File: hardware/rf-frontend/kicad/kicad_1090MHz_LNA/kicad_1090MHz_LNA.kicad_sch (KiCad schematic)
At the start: 11 parts, among them IC1 PGA-103_, X1 STA1090EC

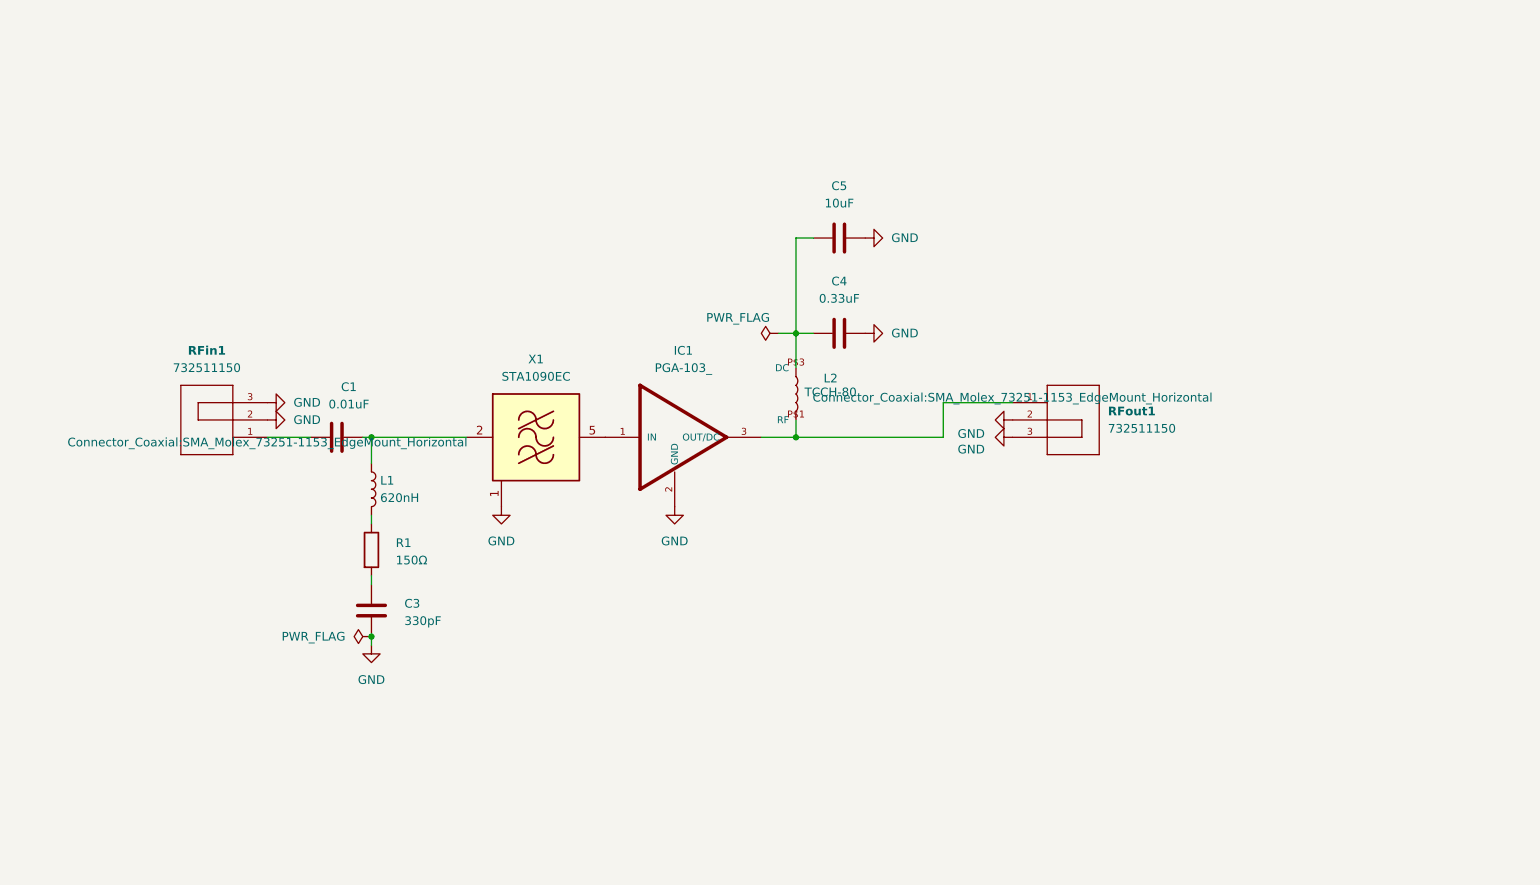
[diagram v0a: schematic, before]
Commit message: Update RF frontend KiCad: completed USB-C LNA board with routing, pours, via stitching, and Gerbers
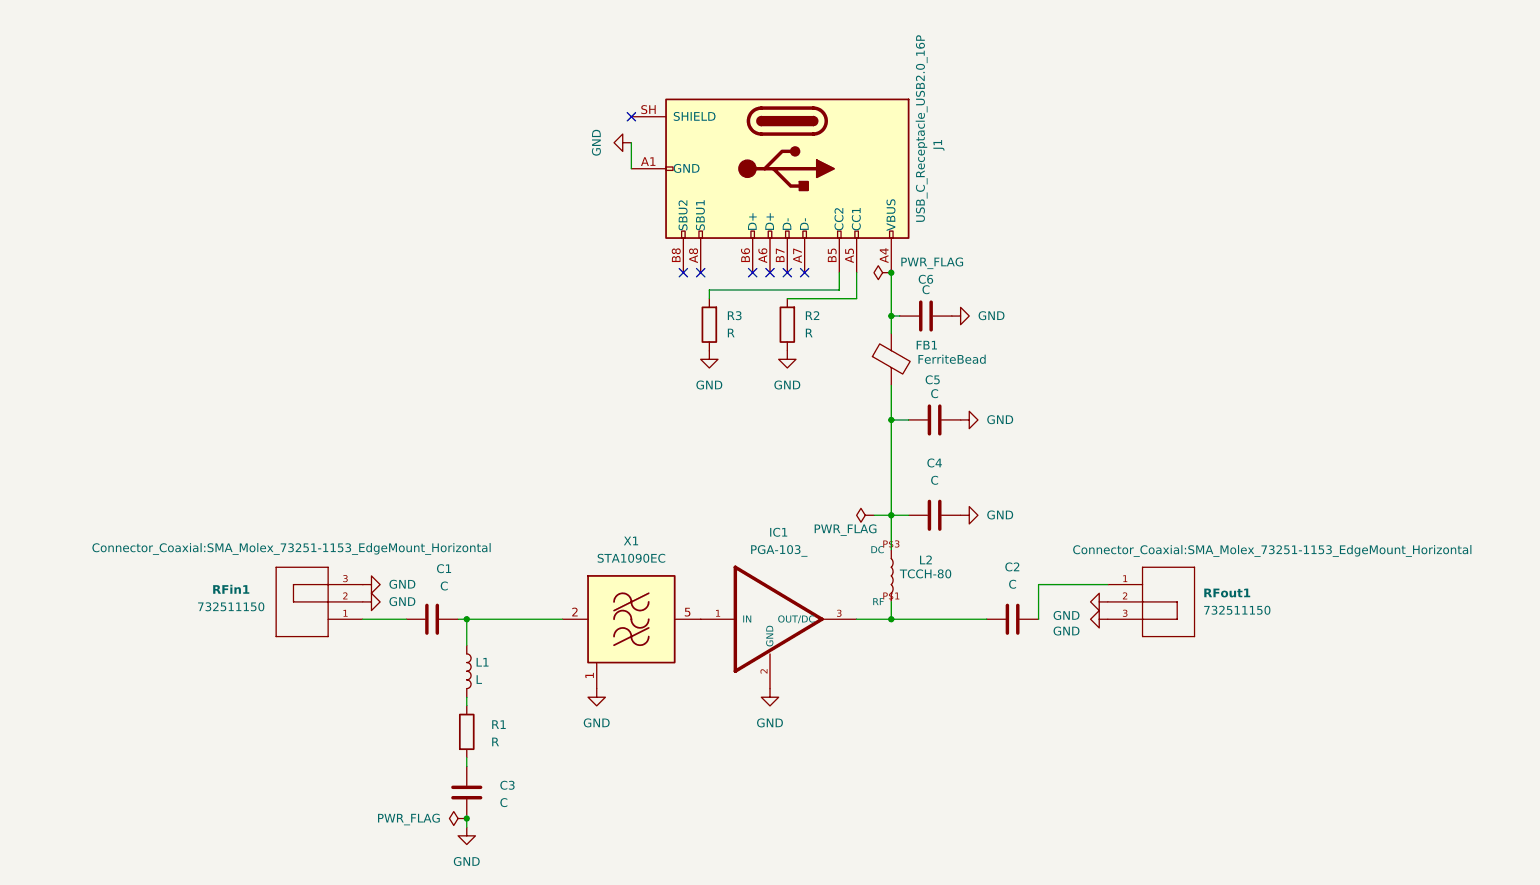
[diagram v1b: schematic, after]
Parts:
- added C2: C, Capacitor_SMD:C_0402_1005Metric, symbol Device:C
- added C6: C, Capacitor_SMD:C_0603_1608Metric, symbol Device:C
- added FB1: FerriteBead, Inductor_SMD:L_0402_1005Metric, symbol Device:FerriteBead
- added J1: USB_C_Receptacle_USB2.0_16P, Connector_USB:USB_C_Receptacle_GCT_USB4085, symbol Connector:USB_C_Receptacle_USB2.0_16P
- added R2, R3: R, Resistor_SMD:R_0402_1005Metric, symbol Device:R
- C1: value 0.01uF -> C
- C3: value 330pF -> C
- C4: value 0.33uF -> C
- C5: value 10uF -> C
- L1: value 620nH -> L
- R1: value 150Ω -> R
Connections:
- net GND: now also C6.2, J1.A1 (GND), J1.A12 (GND), J1.B1 (GND), J1.B12 (GND), R2.1, R3.1
- net at IC1.3 (OUT/DC), L2.P$1 (RF): now also C2.1; no longer RFout1.1
- net at C4.1, C5.1, L2.P$3 (DC): now also FB1.2
- new net: C2.2, RFout1.1
- new net: J1.A5 (CC1), R2.2
- new net: C6.1, FB1.1, J1.A4 (VBUS), J1.A9 (VBUS), J1.B4 (VBUS), J1.B9 (VBUS)
- new net: J1.B5 (CC2), R3.2
- no-connect marks 0 -> 7
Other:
- company: (none) -> Aleksey Mikhno
- title: (none) -> 1090MHz PGA-103+ LNA
- moved on the sheet: C1, C3, C4, C5, IC1, L1, L2, R1, RFin1, RFout1, X1
